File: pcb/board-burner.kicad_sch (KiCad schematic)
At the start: 25 parts, among them J12 DS18B20, J2 TH1, J4 Conn_WallSocket_Earth, J5 Conn_WallSocket_Earth, J7 SSR3, Q10 Q_NMOS_DGS, SW3 RESET, SW4 BOOT, U10 DS18B20, U8 ESP32-S3-WROOM-1

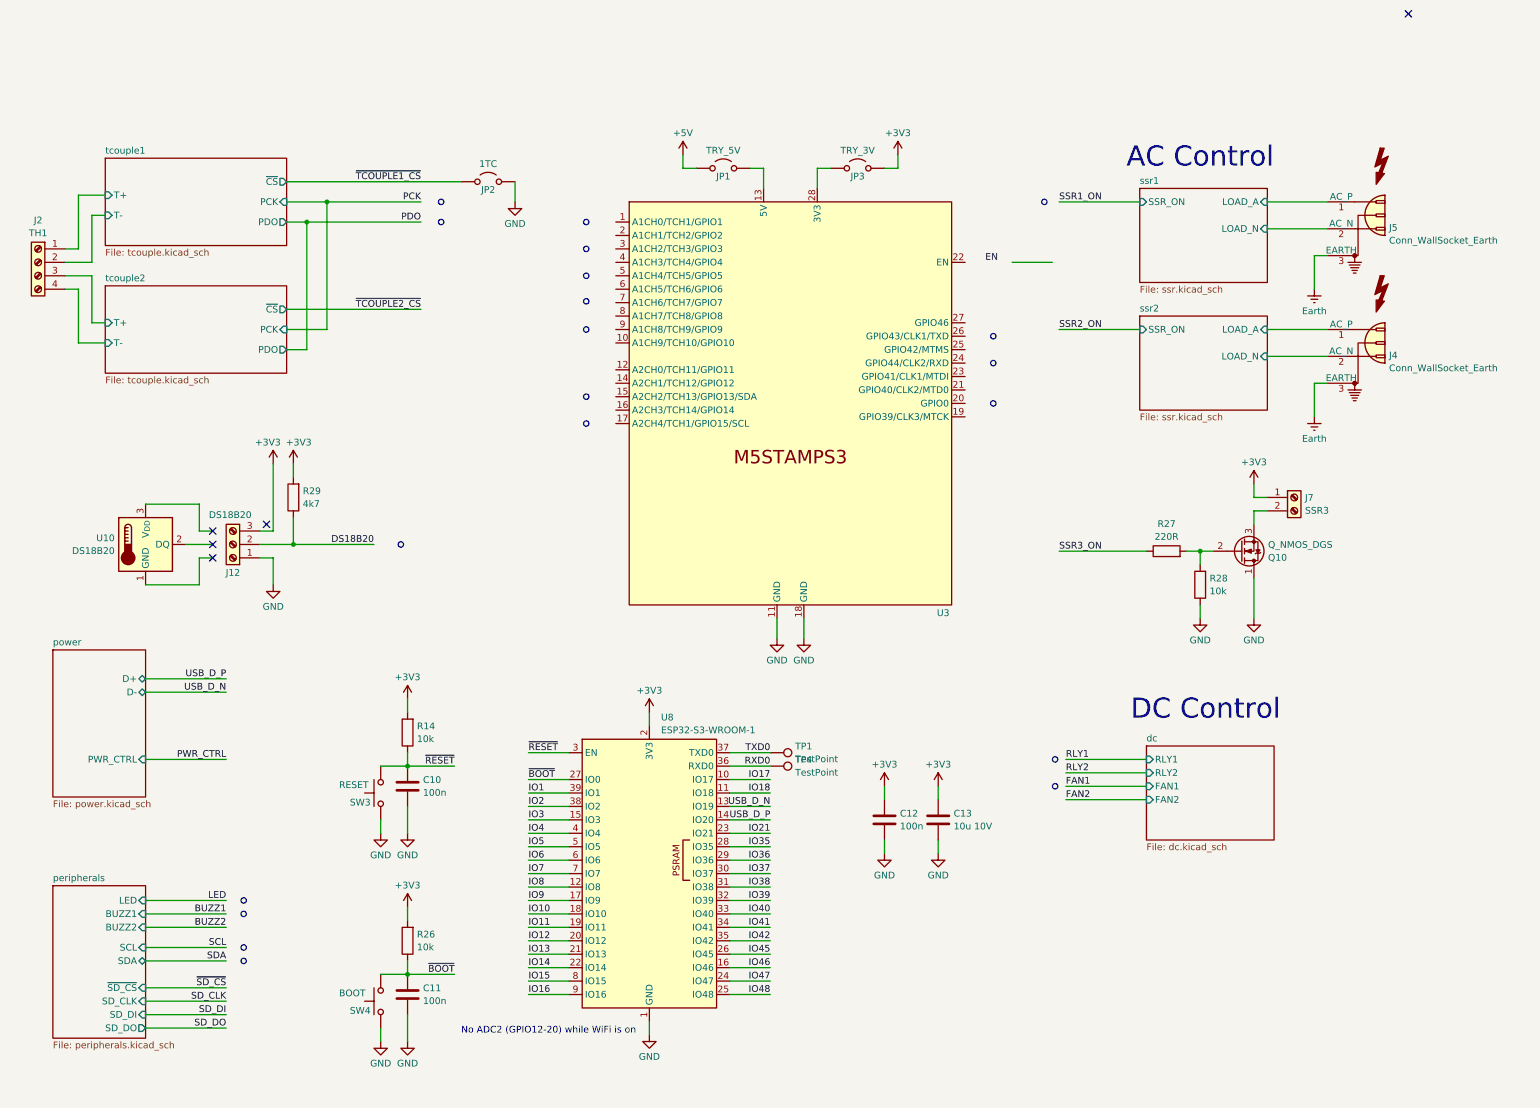
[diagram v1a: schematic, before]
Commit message: Replaced WROOM module symbol with richer version
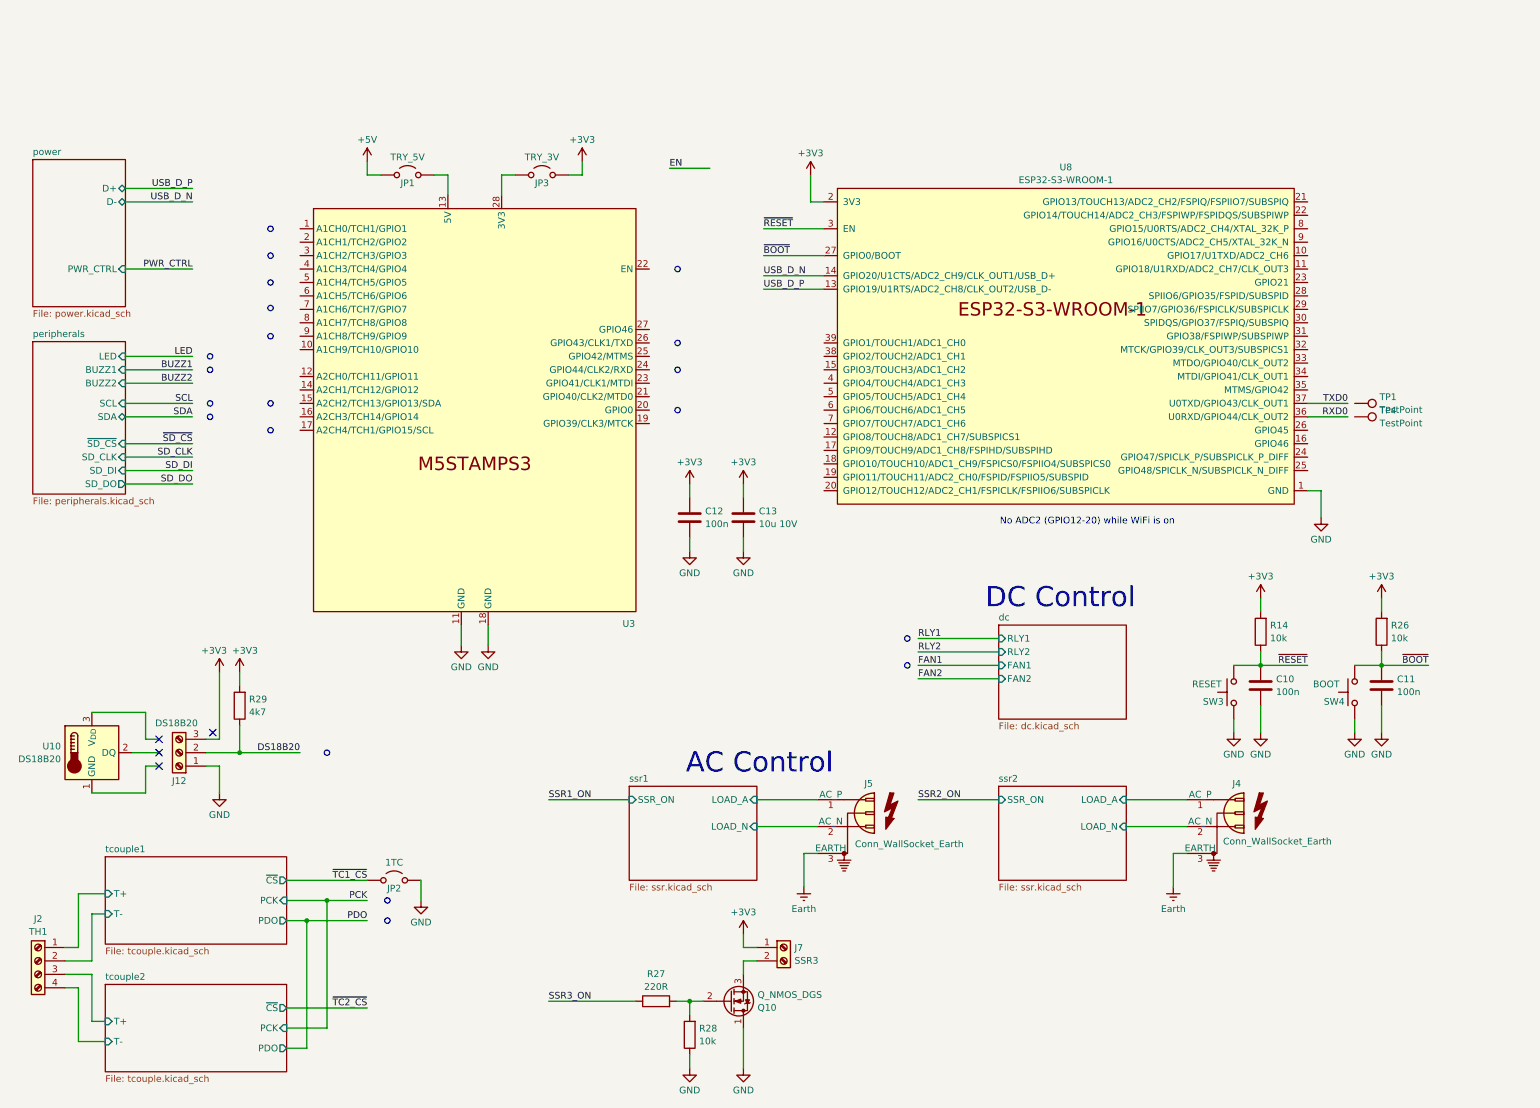
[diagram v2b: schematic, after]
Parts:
- U8: footprint RF_Module:ESP32-S3-WROOM-1 -> Espressif:ESP32-S3-WROOM-1; symbol RF_Module:ESP32-S3-WROOM-1 -> local:ESP32-S3-WROOM-1
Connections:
- net RXD0: no longer TP4.1
- net TXD0: no longer TP1.1
- net USB_D_N: now also U8.14 (GPIO20/U1CTS/ADC2_CH9/CLK_OUT1/USB_D+); no longer U8.13 (IO19)
- net USB_D_P: now also U8.13 (GPIO19/U1RTS/ADC2_CH8/CLK_OUT2/USB_D-); no longer U8.14 (IO20)
- net IO1: no longer names the net of U8.39 (GPIO1/TOUCH1/ADC1_CH0)
- net IO10: no longer names the net of U8.18 (GPIO10/TOUCH10/ADC1_CH9/FSPICS0/FSPIIO4/SUBSPICS0)
- net IO11: no longer names the net of U8.19 (GPIO11/TOUCH11/ADC2_CH0/FSPID/FSPIIO5/SUBSPID)
- net IO12: no longer names the net of U8.20 (GPIO12/TOUCH12/ADC2_CH1/FSPICLK/FSPIIO6/SUBSPICLK)
- net IO13: no longer names the net of U8.21 (GPIO13/TOUCH13/ADC2_CH2/FSPIQ/FSPIIO7/SUBSPIQ)
- net IO14: no longer names the net of U8.22 (GPIO14/TOUCH14/ADC2_CH3/FSPIWP/FSPIDQS/SUBSPIWP)
- net IO15: no longer names the net of U8.8 (GPIO15/U0RTS/ADC2_CH4/XTAL_32K_P)
- net IO16: no longer names the net of U8.9 (GPIO16/U0CTS/ADC2_CH5/XTAL_32K_N)
- net IO17: no longer names the net of U8.10 (GPIO17/U1TXD/ADC2_CH6)
- net IO18: no longer names the net of U8.11 (GPIO18/U1RXD/ADC2_CH7/CLK_OUT3)
- net IO2: no longer names the net of U8.38 (GPIO2/TOUCH2/ADC1_CH1)
- net IO21: no longer names the net of U8.23 (GPIO21)
- net IO3: no longer names the net of U8.15 (GPIO3/TOUCH3/ADC1_CH2)
- net IO35: no longer names the net of U8.28 (SPIIO6/GPIO35/FSPID/SUBSPID)
- net IO36: no longer names the net of U8.29 (SPIIO7/GPIO36/FSPICLK/SUBSPICLK)
- net IO37: no longer names the net of U8.30 (SPIDQS/GPIO37/FSPIQ/SUBSPIQ)
- net IO38: no longer names the net of U8.31 (GPIO38/FSPIWP/SUBSPIWP)
- net IO39: no longer names the net of U8.32 (MTCK/GPIO39/CLK_OUT3/SUBSPICS1)
- net IO4: no longer names the net of U8.4 (GPIO4/TOUCH4/ADC1_CH3)
- net IO40: no longer names the net of U8.33 (MTDO/GPIO40/CLK_OUT2)
- net IO41: no longer names the net of U8.34 (MTDI/GPIO41/CLK_OUT1)
- net IO42: no longer names the net of U8.35 (MTMS/GPIO42)
- net IO45: no longer names the net of U8.26 (GPIO45)
- net IO46: no longer names the net of U8.16 (GPIO46)
- net IO47: no longer names the net of U8.24 (GPIO47/SPICLK_P/SUBSPICLK_P_DIFF)
- net IO48: no longer names the net of U8.25 (GPIO48/SPICLK_N/SUBSPICLK_N_DIFF)
- net IO5: no longer names the net of U8.5 (GPIO5/TOUCH5/ADC1_CH4)
- net IO6: no longer names the net of U8.6 (GPIO6/TOUCH6/ADC1_CH5)
- net IO7: no longer names the net of U8.7 (GPIO7/TOUCH7/ADC1_CH6)
- net IO8: no longer names the net of U8.12 (GPIO8/TOUCH8/ADC1_CH7/SUBSPICS1)
- net IO9: no longer names the net of U8.17 (GPIO9/TOUCH9/ADC1_CH8/FSPIHD/SUBSPIHD)
- net ~{TCOUPLE1_CS} renamed ~{TC1_CS}
- no-connect marks 5 -> 4
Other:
- moved on the sheet: C12, C13, J12, J2, J4, J5, J7, JP1, JP2, JP3, Q10, R27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
